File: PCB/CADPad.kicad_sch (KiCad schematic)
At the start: 30 parts, among them SW1 SW_Push, SW10 RotaryEncoder_Switch, SW2 SW_Push, SW3 SW_Push, SW4 SW_Push, SW5 SW_Push, SW6 SW_Push, SW7 SW_Push, SW8 SW_Push, SW9 SW_Push, U1 XIAO-RP2040-DIP

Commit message: started pcb
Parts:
- OL1: footprint SSD1306_0.91_OLED:SSD1306-0.91-OLED-4pin-128x32 -> Wire_Connectors:SSD1306_0.91_OLED_Wire_Connector
- SW10: footprint Rotary_Encoder:RotaryEncoder_Alps_EC11E-Switch_Vertical_H20mm -> Wire_Connectors:Rotary_Encoder_Wire_Connector
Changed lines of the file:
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@@
 			)
 		)
-		(property "Footprint" "Rotary_Encoder:RotaryEncoder_Alps_EC11E-Switch_Vertical_H20mm"
+		(property "Footprint" "Wire_Connectors:Rotary_Encoder_Wire_Connector"
 			(at 99.06 75.946 0)
 			(effects
@@
 			)
 		)
-		(property "Footprint" "SSD1306_0.91_OLED:SSD1306-0.91-OLED-4pin-128x32"
+		(property "Footprint" "Wire_Connectors:SSD1306_0.91_OLED_Wire_Connector"
 			(at 54.61 76.2 0)
 			(effects

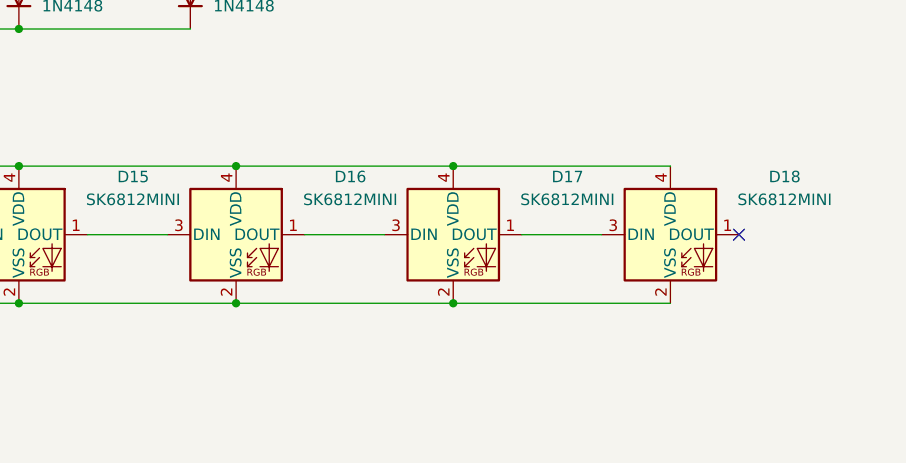
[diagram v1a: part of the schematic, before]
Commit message: made general layout on pcb
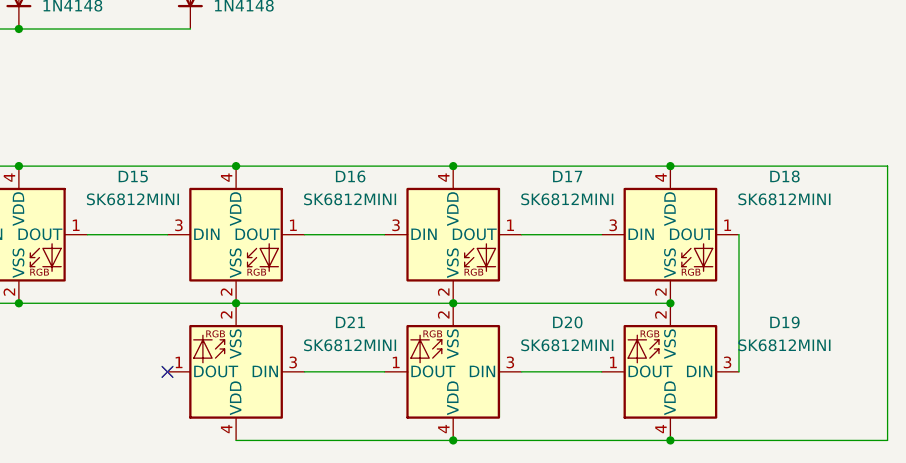
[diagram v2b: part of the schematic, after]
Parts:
- added D19, D20, D21: SK6812MINI, LED_SMD:LED_SK6812MINI_PLCC4_3.5x3.5mm_P1.75mm, symbol LED:SK6812MINI
- U1: footprint OPL:XIAO-RP2040-DIP -> OPL:XIAO-RP2040-SMD
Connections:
- net +5V: now also D19.4 (VDD), D20.4 (VDD), D21.4 (VDD)
- net GND: now also D19.2 (VSS), D20.2 (VSS), D21.2 (VSS)
- net at D18.1 (DOUT): now also D19.3 (DIN)
- new net: D20.1 (DOUT), D21.3 (DIN)
- new net: D19.1 (DOUT), D20.3 (DIN)

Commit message: traced almost everything
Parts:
- U1: footprint OPL:XIAO-RP2040-SMD -> OPL:XIAO-RP2040-DIP
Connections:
- net COL 0: now also U1.11 (GPIO3/MOSI); no longer U1.10 (GPIO4/MISO)
- net COL 1: now also U1.3 (GPIO28/ADC2/A2); no longer U1.9 (GPIO2/SCK)
- net COL 2: now also U1.2 (GPIO27/ADC1/A1); no longer U1.8 (GPIO1/RX)
- net EC11 A: now also U1.7 (GPIO0/TX); no longer U1.4 (GPIO29/ADC3/A3)
- net EC11 B: now also U1.8 (GPIO1/RX); no longer U1.7 (GPIO0/TX)
- net LED: now also U1.1 (GPIO26/ADC0/A0); no longer U1.11 (GPIO3/MOSI)
- net ROW 0: now also U1.4 (GPIO29/ADC3/A3); no longer U1.1 (GPIO26/ADC0/A0)
- net ROW 1: now also U1.10 (GPIO4/MISO); no longer U1.2 (GPIO27/ADC1/A1)
- net ROW 2: now also U1.9 (GPIO2/SCK); no longer U1.3 (GPIO28/ADC2/A2)
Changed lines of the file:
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@@
 	(global_label "EC11 A"
 		(shape input)
-		(at 78.74 44.45 180)
+		(at 78.74 55.88 180)
 		(fields_autoplaced yes)
 		(effects
@@
 		)
 		(property "Intersheetrefs" "${INTERSHEET_REFS}"
-			(at 68.8606 44.45 0)
+			(at 68.8606 55.88 0)
 			(effects
 				(font
@@
 	(global_label "COL 2"
 		(shape input)
-		(at 114.3 55.88 0)
+		(at 78.74 36.83 180)
 		(fields_autoplaced yes)
 		(effects
@@
 				(size 1.27 1.27)
 			)
-			(justify left)
+			(justify right)
 		)
 		(property "Intersheetrefs" "${INTERSHEET_REFS}"
-			(at 123.0909 55.88 0)
+			(at 69.9491 36.83 0)
 			(effects
 				(font
 					(size 1.27 1.27)
 				)
-				(justify left)
+				(justify right)
 				(hide yes)
 			)
@@
 	(global_label "ROW 2"
 		(shape input)
-		(at 78.74 40.64 180)
+		(at 114.3 52.07 0)
 		(fields_autoplaced yes)
 		(effects
@@
 				(size 1.27 1.27)
 			)
-			(justify right)
+			(justify left)
 		)
 		(property "Intersheetrefs" "${INTERSHEET_REFS}"
-			(at 69.5258 40.64 0)
+			(at 123.5142 52.07 0)
 			(effects
 				(font
 					(size 1.27 1.27)
 				)
-				(justify right)
+				(justify left)
 				(hide yes)
 			)
@@
 	(global_label "ROW 1"
 		(shape input)
-		(at 78.74 36.83 180)
+		(at 114.3 48.26 0)
 		(fields_autoplaced yes)
 		(effects
@@
 				(size 1.27 1.27)
 			)
-			(justify right)
+			(justify left)
 		)
 		(property "Intersheetrefs" "${INTERSHEET_REFS}"
-			(at 69.5258 36.83 0)
+			(at 123.5142 48.26 0)
 			(effects
 				(font
 					(size 1.27 1.27)
 				)
-				(justify right)
+				(justify left)
 				(hide yes)
 			)
@@
 	(global_label "COL 1"
 		(shape input)
-		(at 114.3 52.07 0)
+		(at 78.74 40.64 180)
 		(fields_autoplaced yes)
 		(effects
@@
 				(size 1.27 1.27)
 			)
-			(justify left)
+			(justify right)
 		)
 		(property "Intersheetrefs" "${INTERSHEET_REFS}"
-			(at 123.0909 52.07 0)
+			(at 69.9491 40.64 0)
 			(effects
 				(font
 					(size 1.27 1.27)
 				)
-				(justify left)
+				(justify right)
 				(hide yes)
 			)
@@
 	(global_label "ROW 0"
 		(shape input)
-		(at 78.74 33.02 180)
+		(at 78.74 44.45 180)
 		(fields_autoplaced yes)
 		(effects
@@
 		)
 		(property "Intersheetrefs" "${INTERSHEET_REFS}"
-			(at 69.5258 33.02 0)
+			(at 69.5258 44.45 0)
 			(effects
 				(font
@@
 	(global_label "EC11 B"
 		(shape input)
-		(at 78.74 55.88 180)
+		(at 114.3 55.88 0)
 		(fields_autoplaced yes)
 		(effects
@@
 				(size 1.27 1.27)
 			)
-			(justify right)
+			(justify left)
 		)
 		(property "Intersheetrefs" "${INTERSHEET_REFS}"
-			(at 68.6792 55.88 0)
+			(at 124.3608 55.88 0)
 			(effects
 				(font
 					(size 1.27 1.27)
 				)
-				(justify right)
+				(justify left)
 				(hide yes)
 			)
@@
 	(global_label "LED"
 		(shape input)
-		(at 114.3 44.45 0)
+		(at 78.74 33.02 180)
 		(fields_autoplaced yes)
 		(effects
@@
 				(size 1.27 1.27)
 			)
-			(justify left)
+			(justify right)
 		)
 		(property "Intersheetrefs" "${INTERSHEET_REFS}"
-			(at 120.7323 44.45 0)
+			(at 72.3077 33.02 0)
 			(effects
 				(font
 					(size 1.27 1.27)
 				)
-				(justify left)
+				(justify right)
 				(hide yes)
 			)
@@
 	(global_label "COL 0"
 		(shape input)
-		(at 114.3 48.26 0)
+		(at 114.3 44.45 0)
 		(fields_autoplaced yes)
 		(effects
@@
 		)
 		(property "Intersheetrefs" "${INTERSHEET_REFS}"
-			(at 123.0909 48.26 0)
+			(at 123.0909 44.45 0)
 			(effects
 				(font
@@
 			)
 		)
-		(property "Footprint" "OPL:XIAO-RP2040-SMD"
+		(property "Footprint" "OPL:XIAO-RP2040-DIP"
 			(at 97.028 60.198 0)
 			(effects
